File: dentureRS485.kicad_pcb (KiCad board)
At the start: 2 copper layers, 50 x 50 mm, 28 parts, among them J1 Conn_01x04, J2 Conn_01x08, J3 free_holes, J4 Conn_01x08, J5 Conn_01x02, U1 SP3485EN

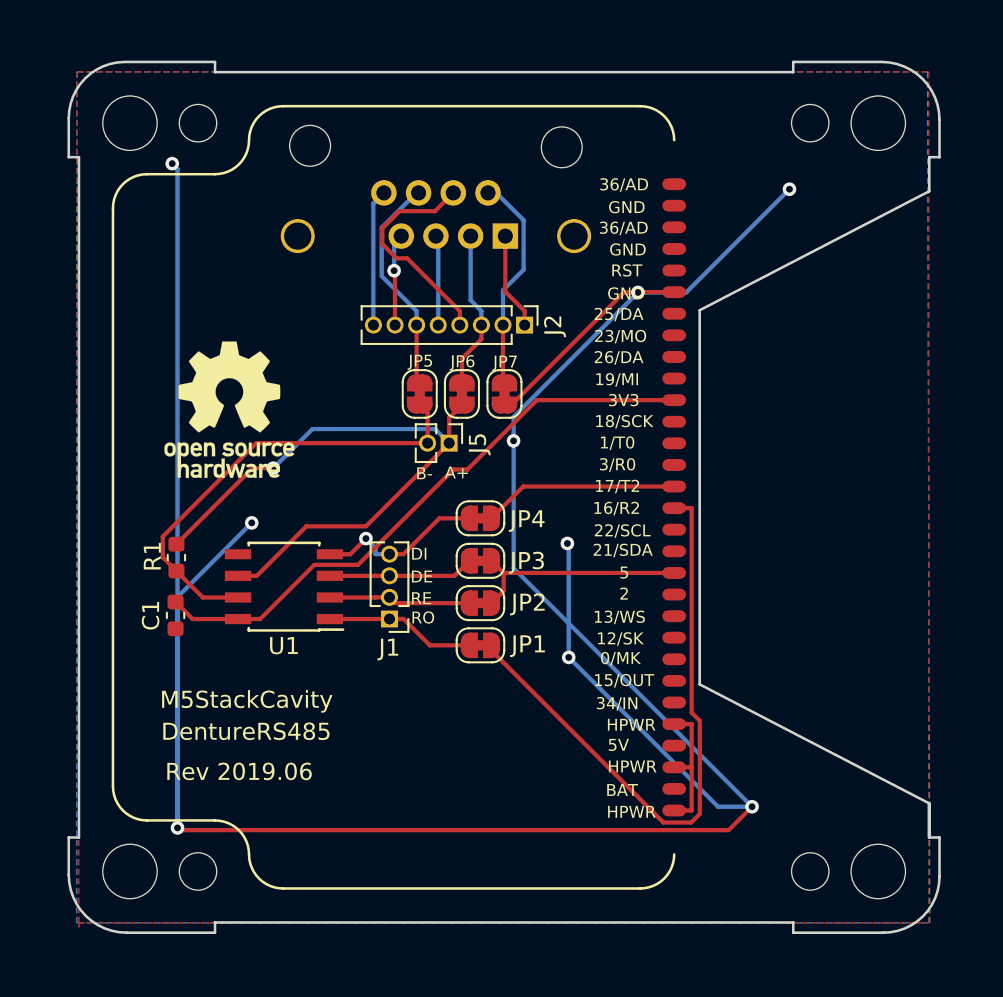
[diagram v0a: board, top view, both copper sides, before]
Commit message: Update outter line for M5Stack outer line
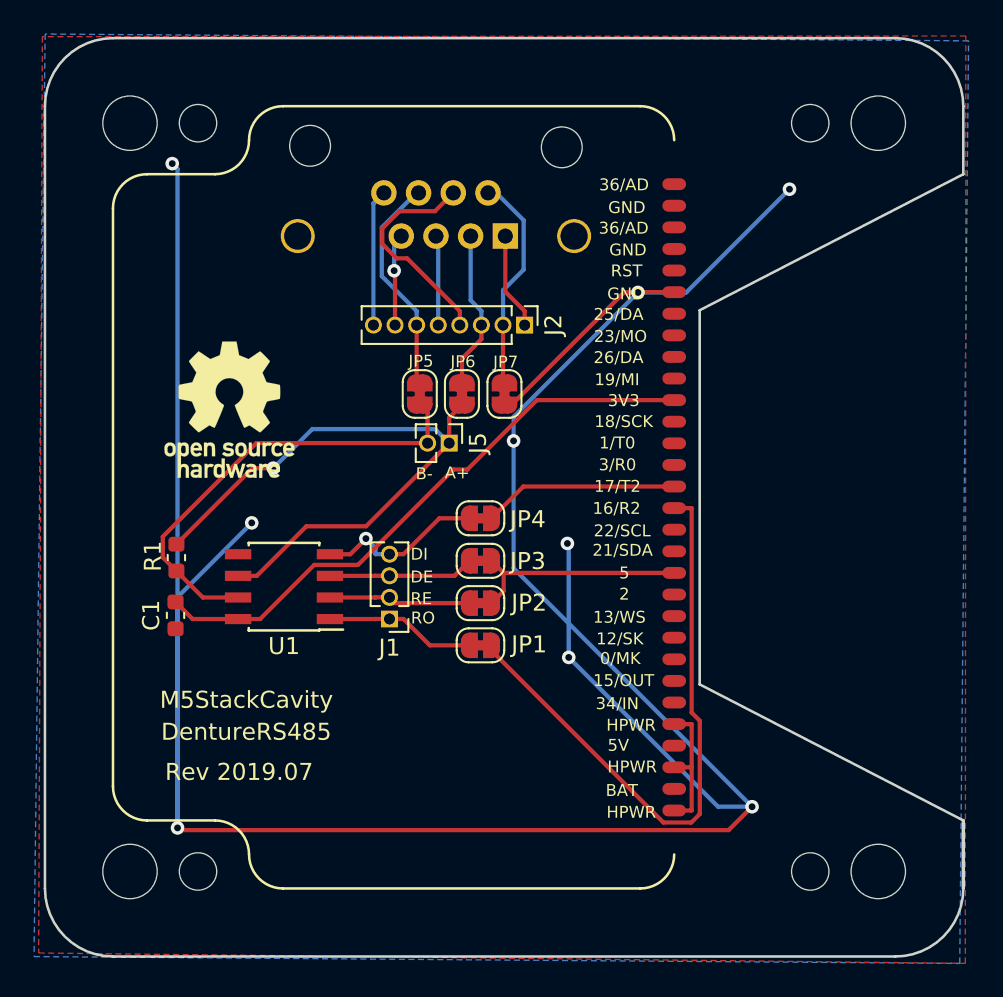
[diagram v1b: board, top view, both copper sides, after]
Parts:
- corner1, corner4: value corner_edge1 -> outer_corner; footprint footprints:corner_edge1 -> footprints:outer_corner
- corner2, corner3: value corner_edge2 -> outer_corner; footprint footprints:corner_edge2 -> footprints:outer_corner
- turned corner2 to 270 degrees
- turned corner3 to 90 degrees
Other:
- board size 50 x 50 mm -> 54 x 54 mm
- board text added: "Rev 2019.07"
- board text removed: "Rev 2019.06"
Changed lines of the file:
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@@
     (add_net "Net-(J2-Pad8)")
+  )
+  (module footprints:outer_corner (layer F.Cu)
+    (at 100 50 90)
+    (fp_text reference corner3 (at -3.9243 -2.4765 90) (layer F.SilkS) hide
+      (effects (font (size 1 1) (thickness 0.15)))
+    )
+    (fp_text value outer_corner (at -3.429 -1.4224 90) (layer F.Fab)
+      (effects (font (size 1 1) (thickness 0.15)))
+    )
+    (fp_arc (start -2 2) (end 2 2) (angle -90) (layer Edge.Cuts) (width 0.15))
+  )
+  (module footprints:outer_corner (layer F.Cu)
+    (at 150 100 270)
+    (fp_text reference corner2 (at -3.9243 -2.4765 90) (layer F.SilkS) hide
+      (effects (font (size 1 1) (thickness 0.15)))
+    )
+    (fp_text value outer_corner (at -3.429 -1.4224 90) (layer F.Fab)
+      (effects (font (size 1 1) (thickness 0.15)))
+    )
+    (fp_arc (start -2 2) (end 2 2) (angle -90) (layer Edge.Cuts) (width 0.15))
+  )
+  (module footprints:outer_corner (layer F.Cu)
+    (at 100 100 180)
+    (fp_text reference corner4 (at -3.9243 -2.4765) (layer F.SilkS) hide
+      (effects (font (size 1 1) (thickness 0.15)))
+    )
+    (fp_text value outer_corner (at -3.429 -1.4224) (layer F.Fab)
+      (effects (font (size 1 1) (thickness 0.15)))
+    )
+    (fp_arc (start -2 2) (end 2 2) (angle -90) (layer Edge.Cuts) (width 0.15))
+  )
+  (module footprints:outer_corner (layer F.Cu)
+    (at 150 50)
+    (fp_text reference corner1 (at -0.4191 -2.6035) (layer F.SilkS) hide
+      (effects (font (size 1 1) (thickness 0.15)))
+    )
+    (fp_text value outer_corner (at -0.0765 -1.6384) (layer F.Fab)
+      (effects (font (size 1 1) (thickness 0.15)))
+    )
+    (fp_arc (start -2 2) (end 2 2) (angle -90) (layer Edge.Cuts) (width 0.15))
   )
   (module Jumper:SolderJumper-2_P1.3mm_Bridged_RoundedPad1.0x1.5mm (layer F.Cu)
@@
       (rotate (xyz 0 0 0))
     )
-  )
-  (module footprints:corner_edge1 (layer F.Cu)
-    (at 100 100 180)
-    (fp_text reference corner4 (at -3.9243 -2.4765) (layer F.SilkS) hide
-      (effects (font (size 1 1) (thickness 0.15)))
-    )
-    (fp_text value corner_edge1 (at -3.429 -1.4224) (layer F.Fab)
-      (effects (font (size 1 1) (thickness 0.15)))
-    )
-    (fp_line (start 0.6 5) (end 0 5) (layer Edge.Cuts) (width 0.15))
-    (fp_line (start 0.6 2.8) (end 0.6 5) (layer Edge.Cuts) (width 0.15))
-    (fp_arc (start -2.8 2.8) (end 0.6 2.8) (angle -90) (layer Edge.Cuts) (width 0.15))
-    (fp_line (start -8 -0.6) (end -2.8 -0.6) (layer Edge.Cuts) (width 0.15))
-    (fp_line (start -8 0) (end -8 -0.6) (layer Edge.Cuts) (width 0.15))
-  )
-  (module footprints:corner_edge1 (layer F.Cu)
-    (at 150 50)
-    (fp_text reference corner1 (at -0.4191 -2.6035) (layer F.SilkS) hide
-      (effects (font (size 1 1) (thickness 0.15)))
-    )
-    (fp_text value corner_edge1 (at -0.0765 -1.6384) (layer F.Fab)
-      (effects (font (size 1 1) (thickness 0.15)))
-    )
-    (fp_line (start 0.6 5) (end 0 5) (layer Edge.Cuts) (width 0.15))
-    (fp_line (start 0.6 2.8) (end 0.6 5) (layer Edge.Cuts) (width 0.15))
-    (fp_arc (start -2.8 2.8) (end 0.6 2.8) (angle -90) (layer Edge.Cuts) (width 0.15))
-    (fp_line (start -8 -0.6) (end -2.8 -0.6) (layer Edge.Cuts) (width 0.15))
-    (fp_line (start -8 0) (end -8 -0.6) (layer Edge.Cuts) (width 0.15))
-  )
-  (module footprints:corner_edge2 (layer F.Cu)
-    (at 100 50)
-    (fp_text reference corner3 (at -3.9243 -2.4765) (layer F.SilkS) hide
-      (effects (font (size 1 1) (thickness 0.15)))
-    )
-    (fp_text value corner_edge2 (at -3.429 -1.4224) (layer F.Fab)
-      (effects (font (size 1 1) (thickness 0.15)))
-    )
-    (fp_line (start -0.6 5) (end 0 5) (layer Edge.Cuts) (width 0.15))
-    (fp_line (start -0.6 2.7) (end -0.6 5) (layer Edge.Cuts) (width 0.15))
-    (fp_arc (start 2.7 2.7) (end -0.6 2.7) (angle 90) (layer Edge.Cuts) (width 0.15))
-    (fp_line (start 8 -0.6) (end 2.7 -0.6) (layer Edge.Cuts) (width 0.15))
-    (fp_line (start 8 0) (end 8 -0.6) (layer Edge.Cuts) (width 0.15))
-  )
-  (module footprints:corner_edge2 (layer F.Cu)
-    (at 150 100 180)
-    (fp_text reference corner2 (at -3.9243 -2.4765) (layer F.SilkS) hide
-      (effects (font (size 1 1) (thickness 0.15)))
-    )
-    (fp_text value corner_edge2 (at -3.429 -1.4224) (layer F.Fab)
-      (effects (font (size 1 1) (thickness 0.15)))
-    )
-    (fp_line (start -0.6 5) (end 0 5) (layer Edge.Cuts) (width 0.15))
-    (fp_line (start -0.6 2.7) (end -0.6 5) (layer Edge.Cuts) (width 0.15))
-    (fp_arc (start 2.7 2.7) (end -0.6 2.7) (angle 90) (layer Edge.Cuts) (width 0.15))
-    (fp_line (start 8 -0.6) (end 2.7 -0.6) (layer Edge.Cuts) (width 0.15))
-    (fp_line (start 8 0) (end 8 -0.6) (layer Edge.Cuts) (width 0.15))
   )
   (module Symbol:OSHW-Logo_7.5x8mm_SilkScreen (layer F.Cu)
@@
     )
   )
-  (gr_line (start 150 55) (end 150 57) (layer Edge.Cuts) (width 0.15))
-  (gr_line (start 136.5 86) (end 150 93) (layer Edge.Cuts) (width 0.15))
+  (gr_line (start 152 52) (end 152 56) (layer Edge.Cuts) (width 0.15))
+  (gr_line (start 136.5 86) (end 152 94) (layer Edge.Cuts) (width 0.15))
   (gr_line (start 136.5 64) (end 136.5 86) (layer Edge.Cuts) (width 0.15))
-  (gr_line (start 150 57) (end 136.5 64) (layer Edge.Cuts) (width 0.15))
+  (gr_line (start 152 56) (end 136.5 64) (layer Edge.Cuts) (width 0.15))
   (gr_text 21/SDA (at 131.9693 78.1131) (layer F.SilkS)
     (effects (font (size 0.7 0.7) (thickness 0.175)))
@@
     (effects (font (size 0.7 0.7) (thickness 0.175)))
   )
-  (gr_line (start 108 50) (end 142 50) (layer Edge.Cuts) (width 0.15))
+  (gr_line (start 102 48) (end 148 48) (layer Edge.Cuts) (width 0.15))
   (gr_arc (start 112 96) (end 110 96) (angle -90) (layer F.SilkS) (width 0.15))
   (gr_arc (start 104 92) (end 102 92) (angle -90) (layer F.SilkS) (width 0.15))
@@
     (effects (font (size 1 1) (thickness 0.25)))
   )
-  (gr_line (start 150 93) (end 150 95) (layer Edge.Cuts) (width 0.2))
+  (gr_line (start 152 94) (end 152 98) (layer Edge.Cuts) (width 0.2))
   (gr_text 34/IN (at 131.6518 87.1301) (layer F.SilkS)
     (effects (font (size 0.7 0.7) (thickness 0.175)))
@@
     (effects (font (size 0.7 0.7) (thickness 0.175)))
   )
-  (gr_text "Rev 2019.06" (at 109.4188 91.1532) (layer F.SilkS)
+  (gr_text "Rev 2019.07" (at 109.4188 91.1532) (layer F.SilkS)
     (effects (font (size 1 1) (thickness 0.25)))
   )
@@
     (effects (font (size 0.7 0.7) (thickness 0.175)))
   )
-  (gr_line (start 100 95) (end 100 55) (layer Edge.Cuts) (width 0.15))
-  (gr_line (start 142 100) (end 108 100) (layer Edge.Cuts) (width 0.15))
+  (gr_line (start 98 98) (end 98 52) (layer Edge.Cuts) (width 0.15))
+  (gr_line (start 148 102) (end 102 102) (layer Edge.Cuts) (width 0.15))
   (via (at 132.8688 62.9532) (size 0.8) (drill 0.4) (layers F.Cu B.Cu) (net 1))
   (segment (start 135 62.935) (end 132.887 62.935) (width 0.25) (layer F.Cu) (net 1))
@@
     (polygon
       (pts
-        (xy 150.0251 100.0252) (xy 149.8981 49.9872) (xy 99.8728 49.9872) (xy 99.8728 100.0252)
+        (xy 151.78959 102.407179) (xy 152.30801 48.159221) (xy 98.011501 47.75719) (xy 97.356622 102.005195)
       )
     )
@@
     (polygon
       (pts
-        (xy 99.8728 49.9872) (xy 99.9998 100.2792) (xy 99.9998 100.0252) (xy 100.7618 100.0252) (xy 149.9743 100.0252)
-        (xy 149.9743 49.9872)
+        (xy 97.8488 47.9132) (xy 97.6288 101.7932) (xy 152.1188 102.4032) (xy 152.1488 47.8732)
       )
     )
